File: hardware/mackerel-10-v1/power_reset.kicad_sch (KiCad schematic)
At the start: 12 parts, among them SW1 SW_Push, U8 NE555P

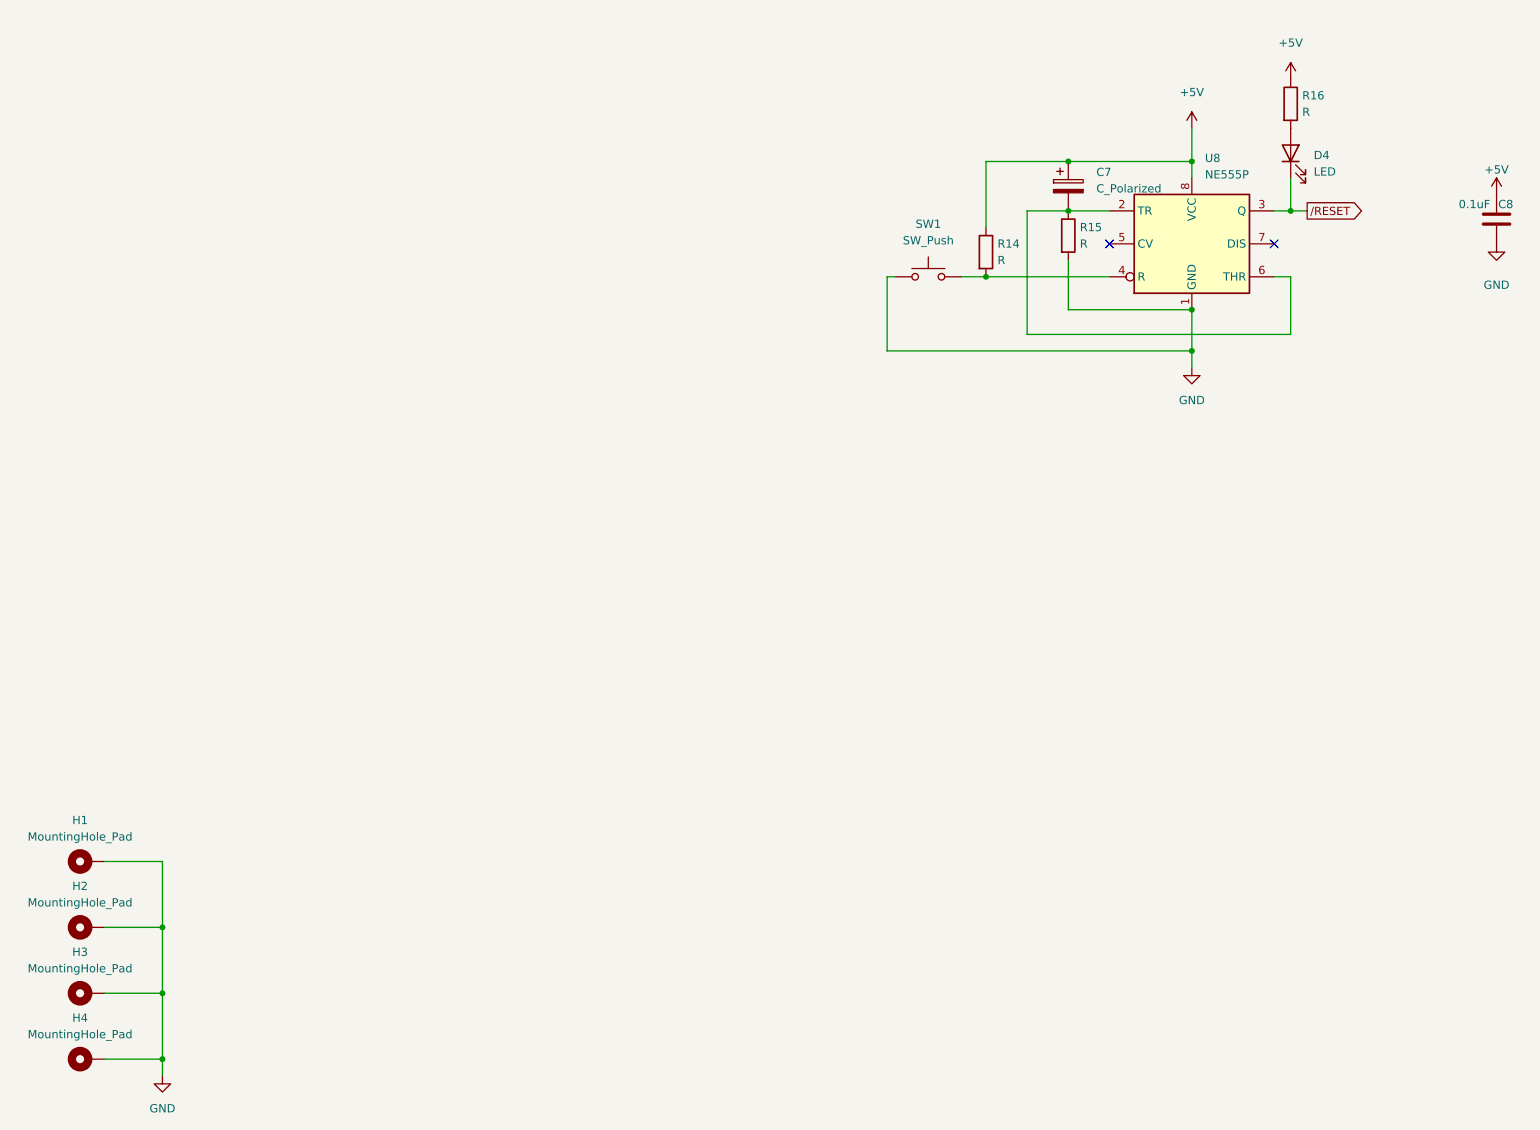
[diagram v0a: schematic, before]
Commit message: Rough layout of components on PCB
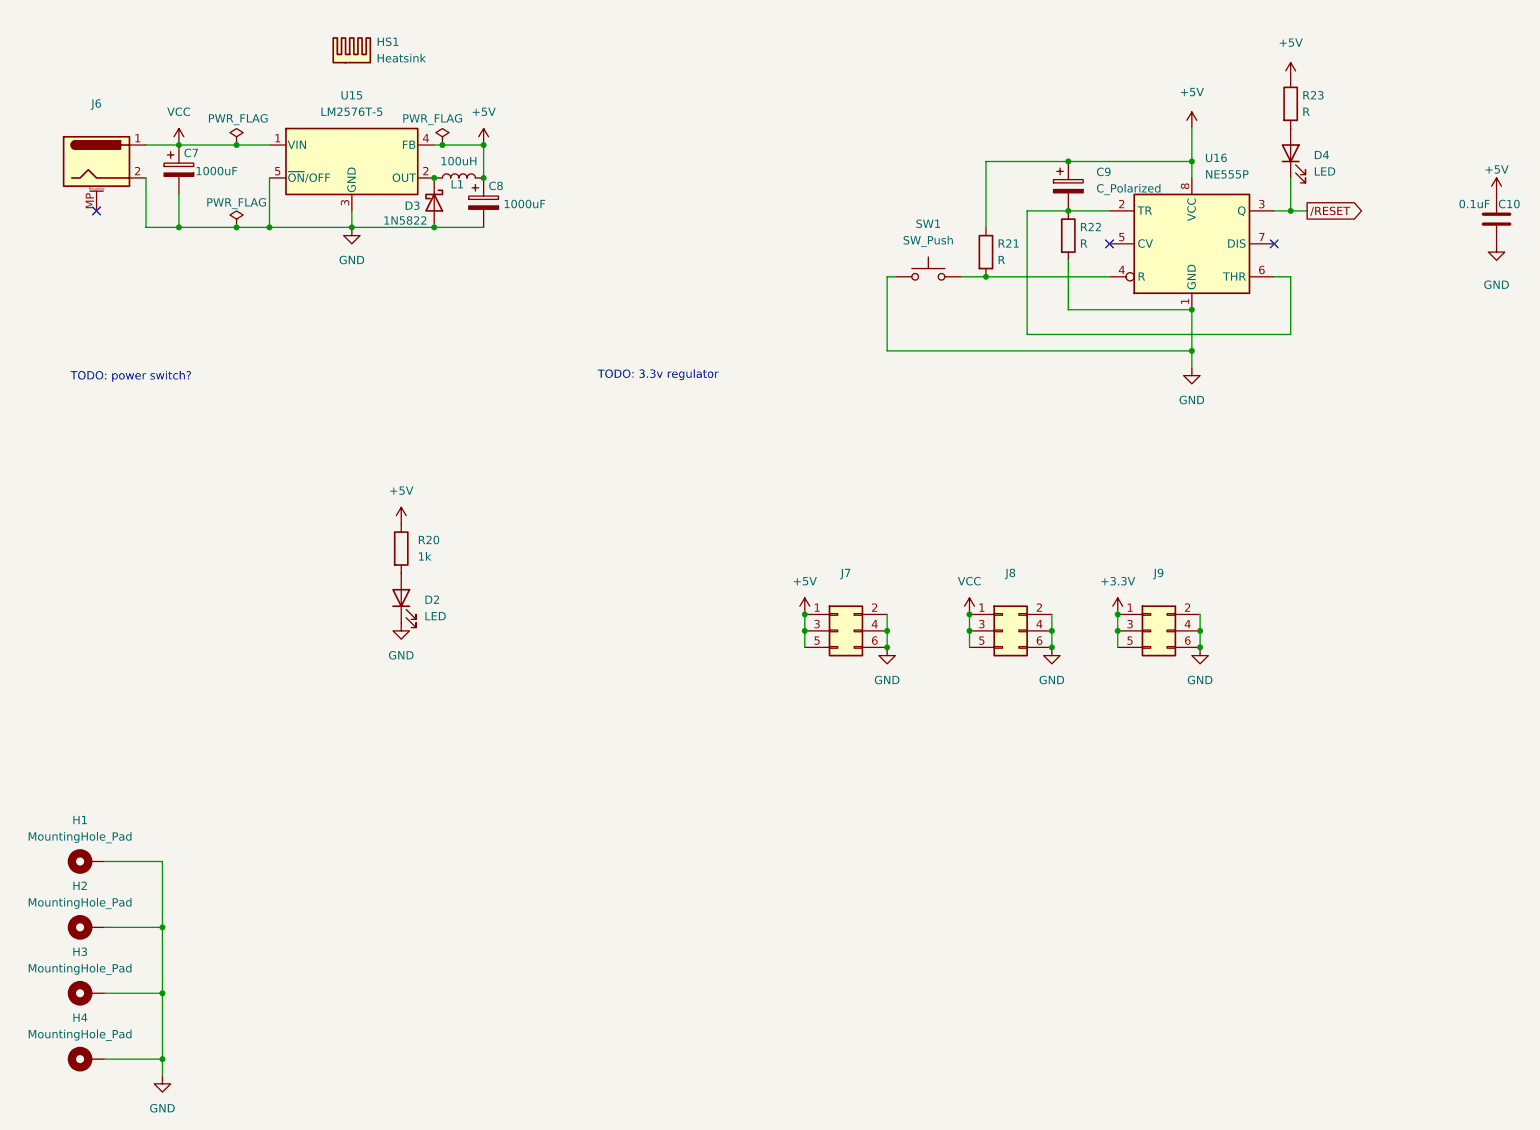
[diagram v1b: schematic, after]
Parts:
- added C7, C8: 1000uF, Capacitor_THT:CP_Radial_D10.0mm_P5.00mm, symbol Device:C_Polarized
- added D2: LED, LED_THT:LED_D5.0mm, symbol Device:LED
- added D3: 1N5822, Diode_THT:D_DO-27_P15.24mm_Horizontal, symbol Device:D_Schottky
- added HS1: Heatsink, Heatsink:Heatsink_Stonecold_HS-S02_13.21x9.53mm, symbol Mechanical:Heatsink
- added J6: Barrel_Jack_MountingPin, Connector_BarrelJack:BarrelJack_Horizontal, symbol Connector:Barrel_Jack_MountingPin
- added J7, J8, J9: Conn_02x03_Odd_Even, Connector_PinHeader_2.54mm:PinHeader_2x03_P2.54mm_Vertical, symbol Connector_Generic:Conn_02x03_Odd_Even
- added L1: 100uH, Inductor_THT:L_Radial_D10.0mm_P5.00mm_Fastron_07M, symbol Device:L
- added R20: 1k, Resistor_THT:R_Axial_DIN0207_L6.3mm_D2.5mm_P7.62mm_Horizontal, symbol Device:R
- added U15: LM2576T-5, Package_TO_SOT_THT:TO-220-5_Vertical, symbol Regulator_Switching:LM2576T-5
- R21: renamed from R14; footprint Resistor_THT:R_Axial_DIN0204_L3.6mm_D1.6mm_P5.08mm_Horizontal -> Resistor_THT:R_Axial_DIN0207_L6.3mm_D2.5mm_P7.62mm_Horizontal
- R22: renamed from R15; footprint Resistor_THT:R_Axial_DIN0204_L3.6mm_D1.6mm_P5.08mm_Horizontal -> Resistor_THT:R_Axial_DIN0207_L6.3mm_D2.5mm_P7.62mm_Horizontal
- R23: renamed from R16; footprint Resistor_THT:R_Axial_DIN0204_L3.6mm_D1.6mm_P5.08mm_Horizontal -> Resistor_THT:R_Axial_DIN0207_L6.3mm_D2.5mm_P7.62mm_Horizontal
- renumbered C8 to C10, C7 to C9, U8 to U16
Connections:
- net +5V: now also C8.1, J7.1 (Pin_1), J7.3 (Pin_3), J7.5 (Pin_5), L1.2, R20.1, U15.4 (FB)
- net GND: now also C7.2, C8.2, D2.1 (K), D3.2 (A), J6.2, J7.2 (Pin_2), J7.4 (Pin_4), J7.6 (Pin_6), J8.2 (Pin_2), J8.4 (Pin_4), J8.6 (Pin_6), J9.2 (Pin_2), J9.4 (Pin_4), J9.6 (Pin_6), U15.3 (GND), U15.5 (~{ON}/OFF)
- new net: D3.1 (K), L1.1, U15.2 (OUT)
- new net: D2.2 (A), R20.2
- new net +3.3V: J9.1 (Pin_1), J9.3 (Pin_3), J9.5 (Pin_5)
- new net VCC: C7.1, J6.1, J8.1 (Pin_1), J8.3 (Pin_3), J8.5 (Pin_5), U15.1 (VIN)
- no-connect marks 2 -> 3
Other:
- note added: "TODO: 3.3v regulator"
- note added: "TODO: power switch?"

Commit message: Settled on mini ITX form factor
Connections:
- net VCC renamed +12V
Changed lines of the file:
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@@
 	)
 	(junction
+		(at 168.91 115.57)
+		(diameter 0)
+		(color 0 0 0 0)
+	)
+	(junction
 		(at 86.36 55.88)
 		(diameter 0)
@@
 		(color 0 0 0 0)
 	)
-	(junction
-		(at 168.91 115.57)
-		(diameter 0)
-		(color 0 0 0 0)
-	)
 	(no_connect
 		(at 215.9 58.42)
@@
 	)
 	(symbol
+		(lib_id "power:+12V")
+		(at 46.99 43.18 0)
+		(unit 1)
+		(exclude_from_sim no)
+		(in_bom yes)
+		(on_board yes)
+		(dnp no)
+		(fields_autoplaced yes)
+		(property "Reference" "#PWR062"
+			(at 46.99 46.99 0)
+			(effects
+				(font
+					(size 1.27 1.27)
+				)
+				(hide yes)
+			)
+		)
+		(property "Value" "+12V"
+			(at 46.99 38.1 0)
+			(effects
+				(font
+					(size 1.27 1.27)
+				)
+			)
+		)
+		(property "Footprint" ""
+			(at 46.99 43.18 0)
+			(effects
+				(font
+					(size 1.27 1.27)
+				)
+				(hide yes)
+			)
+		)
+		(property "Datasheet" ""
+			(at 46.99 43.18 0)
+			(effects
+				(font
+					(size 1.27 1.27)
+				)
+				(hide yes)
+			)
+		)
+		(property "Description" "Power symbol creates a global label with name \"+12V\""
+			(at 46.99 43.18 0)
+			(effects
+				(font
+					(size 1.27 1.27)
+				)
+				(hide yes)
+			)
+		)
+		(pin "1"
+		)
+		(instances
+			(project ""
+				(path "/0a8f74be-008b-4256-a2d9-73a458311ea0/8aeb3dd0-e160-42fa-9696-775a77424698"
+					(reference "#PWR062")
+					(unit 1)
+				)
+			)
+		)
+	)
+	(symbol
 		(lib_id "Regulator_Switching:LM2576T-5")
 		(at 73.66 45.72 0)
@@
 	)
 	(symbol
+		(lib_id "power:+12V")
+		(at 168.91 115.57 0)
+		(unit 1)
+		(exclude_from_sim no)
+		(in_bom yes)
+		(on_board yes)
+		(dnp no)
+		(fields_autoplaced yes)
+		(property "Reference" "#PWR069"
+			(at 168.91 119.38 0)
+			(effects
+				(font
+					(size 1.27 1.27)
+				)
+				(hide yes)
+			)
+		)
+		(property "Value" "+12V"
+			(at 168.91 110.49 0)
+			(effects
+				(font
+					(size 1.27 1.27)
+				)
+			)
+		)
+		(property "Footprint" ""
+			(at 168.91 115.57 0)
+			(effects
+				(font
+					(size 1.27 1.27)
+				)
+				(hide yes)
+			)
+		)
+		(property "Datasheet" ""
+			(at 168.91 115.57 0)
+			(effects
+				(font
+					(size 1.27 1.27)
+				)
+				(hide yes)
+			)
+		)
+		(property "Description" "Power symbol creates a global label with name \"+12V\""
+			(at 168.91 115.57 0)
+			(effects
+				(font
+					(size 1.27 1.27)
+				)
+				(hide yes)
+			)
+		)
+		(pin "1"
+		)
+		(instances
+			(project ""
+				(path "/0a8f74be-008b-4256-a2d9-73a458311ea0/8aeb3dd0-e160-42fa-9696-775a77424698"
+					(reference "#PWR069")
+					(unit 1)
+				)
+			)
+		)
+	)
+	(symbol
 		(lib_id "power:+5V")
 		(at 218.44 33.02 0)
@@
 	)
 	(symbol
-		(lib_id "power:VCC")
-		(at 46.99 43.18 0)
-		(unit 1)
-		(exclude_from_sim no)
-		(in_bom yes)
-		(on_board yes)
-		(dnp no)
-		(fields_autoplaced yes)
-		(property "Reference" "#PWR062"
-			(at 46.99 46.99 0)
-			(effects
-				(font
-					(size 1.27 1.27)
-				)
-				(hide yes)
-			)
-		)
-		(property "Value" "VCC"
-			(at 46.99 38.1 0)
-			(effects
-				(font
-					(size 1.27 1.27)
-				)
-			)
-		)
-		(property "Footprint" ""
-			(at 46.99 43.18 0)
-			(effects
-				(font
-					(size 1.27 1.27)
-				)
-				(hide yes)
-			)
-		)
-		(property "Datasheet" ""
-			(at 46.99 43.18 0)
-			(effects
-				(font
-					(size 1.27 1.27)
-				)
-				(hide yes)
-			)
-		)
-		(property "Description" "Power symbol creates a global label with name \"VCC\""
-			(at 46.99 43.18 0)
-			(effects
-				(font
-					(size 1.27 1.27)
-				)
-				(hide yes)
-			)
-		)
-		(pin "1"
-		)
-		(instances
-			(project "mackerel-10-v1"
-				(path "/0a8f74be-008b-4256-a2d9-73a458311ea0/8aeb3dd0-e160-42fa-9696-775a77424698"
-					(reference "#PWR062")
-					(unit 1)
-				)
-			)
-		)
-	)
-	(symbol
 		(lib_id "Device:D_Schottky")
 		(at 86.36 52.07 270)
@@
 					(unit 1)
 				)
-			)
-		)
-	)
-	(symbol
-		(lib_id "power:VCC")
-		(at 168.91 115.57 0)
-		(unit 1)
-		(exclude_from_sim no)
-		(in_bom yes)
-		(on_board yes)
-		(dnp no)
-		(fields_autoplaced yes)
-		(property "Reference" "#PWR069"
-			(at 168.91 119.38 0)
-			(effects
-				(font
-					(size 1.27 1.27)
-				)
-				(hide yes)
-			)
-		)
-		(property "Value" "VCC"
-			(at 168.91 110.49 0)
-			(effects
-				(font
-					(size 1.27 1.27)
-				)
-			)
-		)
-		(property "Footprint" ""
-			(at 168.91 115.57 0)
-			(effects
-				(font
-					(size 1.27 1.27)
-				)
-				(hide yes)
-			)
-		)
-		(property "Datasheet" ""
-			(at 168.91 115.57 0)
-			(effects
-				(font
-					(size 1.27 1.27)
-				)
-				(hide yes)
-			)
-		)
-		(property "Description" "Power symbol creates a global label with name \"VCC\""
-			(at 168.91 115.57 0)
-			(effects
-				(font
-					(size 1.27 1.27)
-				)
-				(hide yes)
-			)
-		)
-		(pin "1"
-		)
-		(instances
-			(project "mackerel-10-v1"
-				(path "/0a8f74be-008b-4256-a2d9-73a458311ea0/8aeb3dd0-e160-42fa-9696-775a77424698"
-					(reference "#PWR069")
-					(unit 1)
-				)

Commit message: Another layout plan
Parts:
- removed C10: 0.1uF, Capacitor_THT:C_Disc_D4.7mm_W2.5mm_P5.00mm, symbol Device:C
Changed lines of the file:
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@@
-	(symbol
-		(lib_id "power:GND")
-		(at 250.19 58.42 0)
-		(unit 1)
-		(exclude_from_sim no)
-		(in_bom yes)
-		(on_board yes)
-		(dnp no)
-		(fields_autoplaced yes)
-		(property "Reference" "#PWR077"
-			(at 250.19 64.77 0)
-			(effects
-				(font
-					(size 1.27 1.27)
-				)
-				(hide yes)
-			)
-		)
-		(property "Value" "GND"
-			(at 250.19 64.77 0)
-			(effects
-				(font
-					(size 1.27 1.27)
-				)
-			)
-		)
-		(property "Footprint" ""
-			(at 250.19 58.42 0)
-			(effects
-				(font
-					(size 1.27 1.27)
-				)
-				(hide yes)
-			)
-		)
-		(property "Datasheet" ""
-			(at 250.19 58.42 0)
-			(effects
-				(font
-					(size 1.27 1.27)
-				)
-				(hide yes)
-			)
-		)
-		(property "Description" "Power symbol creates a global label with name \"GND\" , ground"
-			(at 250.19 58.42 0)
-			(effects
-				(font
-					(size 1.27 1.27)
-				)
-				(hide yes)
-			)
-		)
-		(pin "1"
-		)
-		(instances
-			(project "mackerel-10-v1"
-				(path "/0a8f74be-008b-4256-a2d9-73a458311ea0/8aeb3dd0-e160-42fa-9696-775a77424698"
-					(reference "#PWR077")
-					(unit 1)
-				)
-			)
-		)
-	)
 	(symbol
 		(lib_id "power:GND")
@@
 	)
 	(symbol
-		(lib_id "power:+5V")
-		(at 250.19 50.8 0)
-		(unit 1)
-		(exclude_from_sim no)
-		(in_bom yes)
-		(on_board yes)
-		(dnp no)
-		(fields_autoplaced yes)
-		(property "Reference" "#PWR076"
-			(at 250.19 54.61 0)
-			(effects
-				(font
-					(size 1.27 1.27)
-				)
-				(hide yes)
-			)
-		)
-		(property "Value" "+5V"
-			(at 250.19 46.99 0)
-			(effects
-				(font
-					(size 1.27 1.27)
-				)
-			)
-		)
-		(property "Footprint" ""
-			(at 250.19 50.8 0)
-			(effects
-				(font
-					(size 1.27 1.27)
-				)
-				(hide yes)
-			)
-		)
-		(property "Datasheet" ""
-			(at 250.19 50.8 0)
-			(effects
-				(font
-					(size 1.27 1.27)
-				)
-				(hide yes)
-			)
-		)
-		(property "Description" "Power symbol creates a global label with name \"+5V\""
-			(at 250.19 50.8 0)
-			(effects
-				(font
-					(size 1.27 1.27)
-				)
-				(hide yes)
-			)
-		)
-		(pin "1"
-		)
-		(instances
-			(project "mackerel-10-v1"
-				(path "/0a8f74be-008b-4256-a2d9-73a458311ea0/8aeb3dd0-e160-42fa-9696-775a77424698"
-					(reference "#PWR076")
-					(unit 1)
-				)
-			)
-		)
-	)
-	(symbol
 		(lib_id "Device:L")
 		(at 90.17 48.26 90)
@@
 					(unit 1)
 				)
-			)
-		)
-	)
-	(symbol
-		(lib_id "Device:C")
-		(at 250.19 54.61 0)
-		(unit 1)
-		(exclude_from_sim no)
-		(in_bom yes)
-		(on_board yes)
-		(dnp no)
-		(property "Reference" "C10"
-			(at 250.444 52.324 0)
-			(effects
-				(font
-					(size 1.27 1.27)
-				)
-				(justify left)
-			)
-		)
-		(property "Value" "0.1uF"
-			(at 244.348 52.324 0)
-			(effects
-				(font
-					(size 1.27 1.27)
-				)
-				(justify left)
-			)
-		)
-		(property "Footprint" "Capacitor_THT:C_Disc_D4.7mm_W2.5mm_P5.00mm"
-			(at 251.1552 58.42 0)
-			(effects
-				(font
-					(size 1.27 1.27)
-				)
-				(hide yes)
-			)
-		)
-		(property "Datasheet" "~"
-			(at 250.19 54.61 0)
-			(effects
-				(font
-					(size 1.27 1.27)
-				)
-				(hide yes)
-			)
-		)
-		(property "Description" "Unpolarized capacitor"
-			(at 250.19 54.61 0)
-			(effects
-				(font
-					(size 1.27 1.27)
-				)
-				(hide yes)
-			)
-		)
-		(pin "2"
-		)
-		(pin "1"
-		)
-		(instances
-			(project "mackerel-10-v1"
-				(path "/0a8f74be-008b-4256-a2d9-73a458311ea0/8aeb3dd0-e160-42fa-9696-775a77424698"
-					(reference "C10")
-					(unit 1)
-				)

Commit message: half routed
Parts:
- added C22: C, Capacitor_THT:C_Disc_D4.3mm_W1.9mm_P5.00mm, symbol Device:C
- H1, H2, H3, H4: footprint MountingHole:MountingHole_3.2mm_M3_Pad -> MountingHole:MountingHole_3.2mm_M3_Pad_Via
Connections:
- net +5V: now also C22.1
- net GND: now also C22.2

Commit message: Mostly routed except expansion
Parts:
- removed J9: Conn_02x03_Odd_Even, Connector_PinHeader_2.54mm:PinHeader_2x03_P2.54mm_Vertical, symbol Connector_Generic:Conn_02x03_Odd_Even
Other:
- note removed: "TODO: 3.3v regulator"

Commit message: IDE interface routed
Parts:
- removed J7: Conn_02x03_Odd_Even, Connector_PinHeader_2.54mm:PinHeader_2x03_P2.54mm_Vertical, symbol Connector_Generic:Conn_02x03_Odd_Even

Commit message: Mack-10 v1 fully routed
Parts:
- added C48, C49: 10uF, Capacitor_THT:CP_Radial_D5.0mm_P2.00mm, symbol Device:C_Polarized_US
- added J10, J11: Conn_02x03_Odd_Even, Connector_PinHeader_2.54mm:PinHeader_2x03_P2.54mm_Vertical, symbol Connector_Generic:Conn_02x03_Odd_Even
- added U17: AMS1117-3.3, Package_TO_SOT_SMD:SOT-223-3_TabPin2, symbol Regulator_Linear:AMS1117-3.3
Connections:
- net +5V: now also C48.1, J10.1 (Pin_1), J10.3 (Pin_3), J10.5 (Pin_5), U17.3 (VI)
- net GND: now also C48.2, C49.2, J10.2 (Pin_2), J10.4 (Pin_4), J10.6 (Pin_6), J11.2 (Pin_2), J11.4 (Pin_4), J11.6 (Pin_6), U17.1 (GND)
- new net +3.3V: C49.1, J11.1 (Pin_1), J11.3 (Pin_3), J11.5 (Pin_5), U17.2 (VO)

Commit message: Mackerel-10 v1 release
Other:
- note removed: "TODO: power switch?"
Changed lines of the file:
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@@
-		)
-	)
-	(text "TODO: power switch?"
-		(exclude_from_sim no)
-		(at 39.624 78.994 0)
-		(effects
-			(font
-				(size 1.27 1.27)
-			)
 		)
 	)
